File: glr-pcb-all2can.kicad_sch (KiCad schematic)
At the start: 0 parts

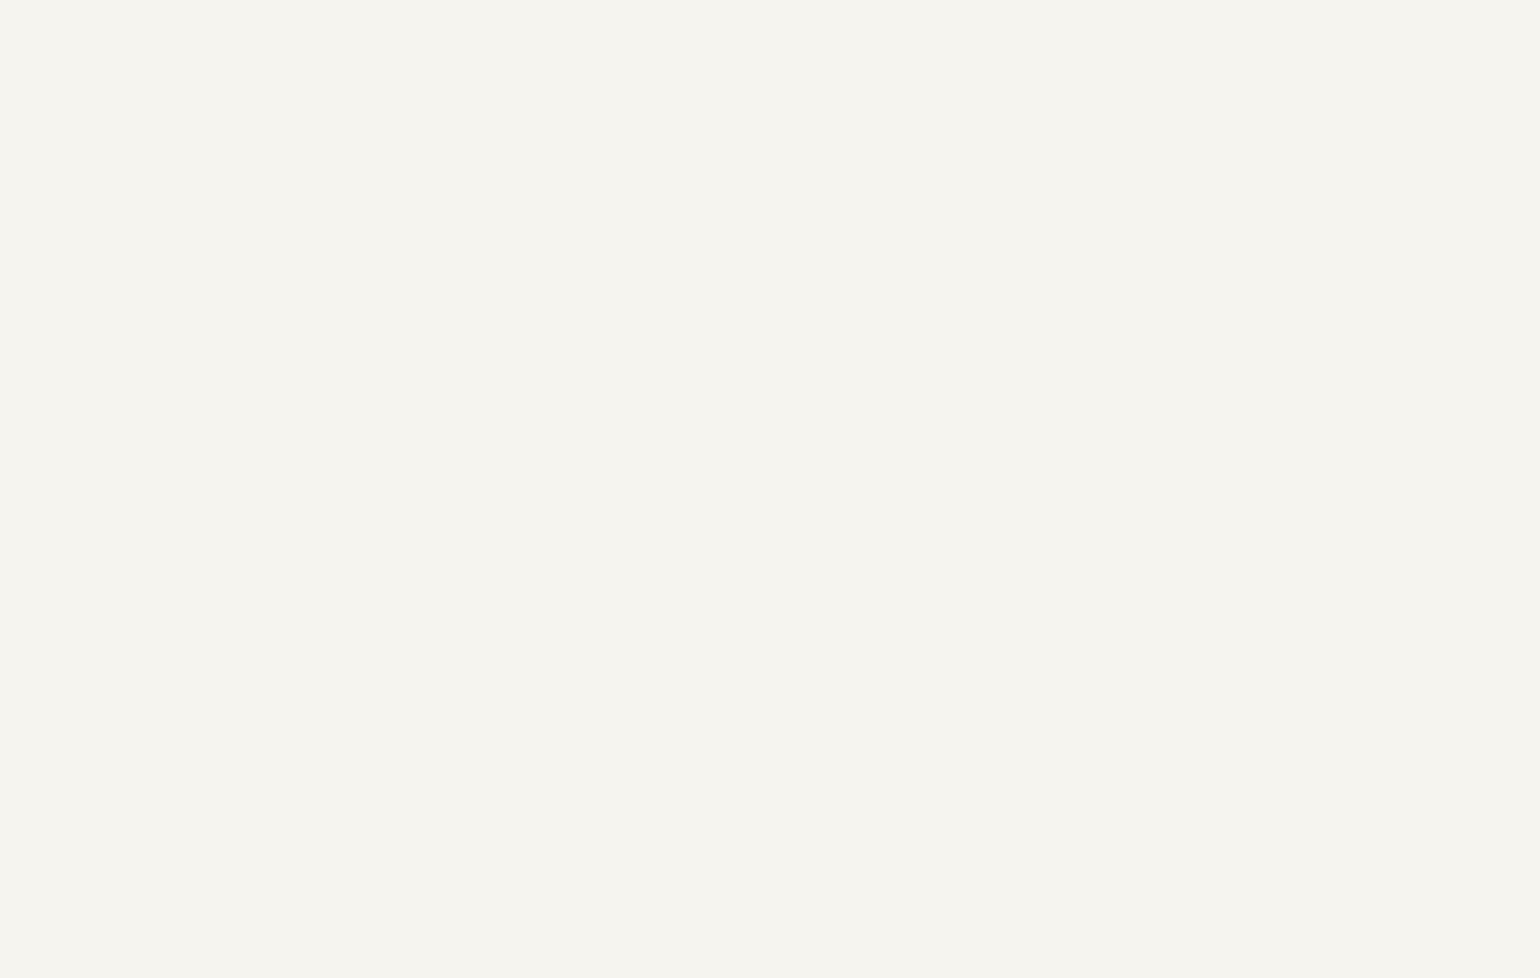
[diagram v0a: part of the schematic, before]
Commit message: add first can transcievers
update to glr-pcb-all2can references
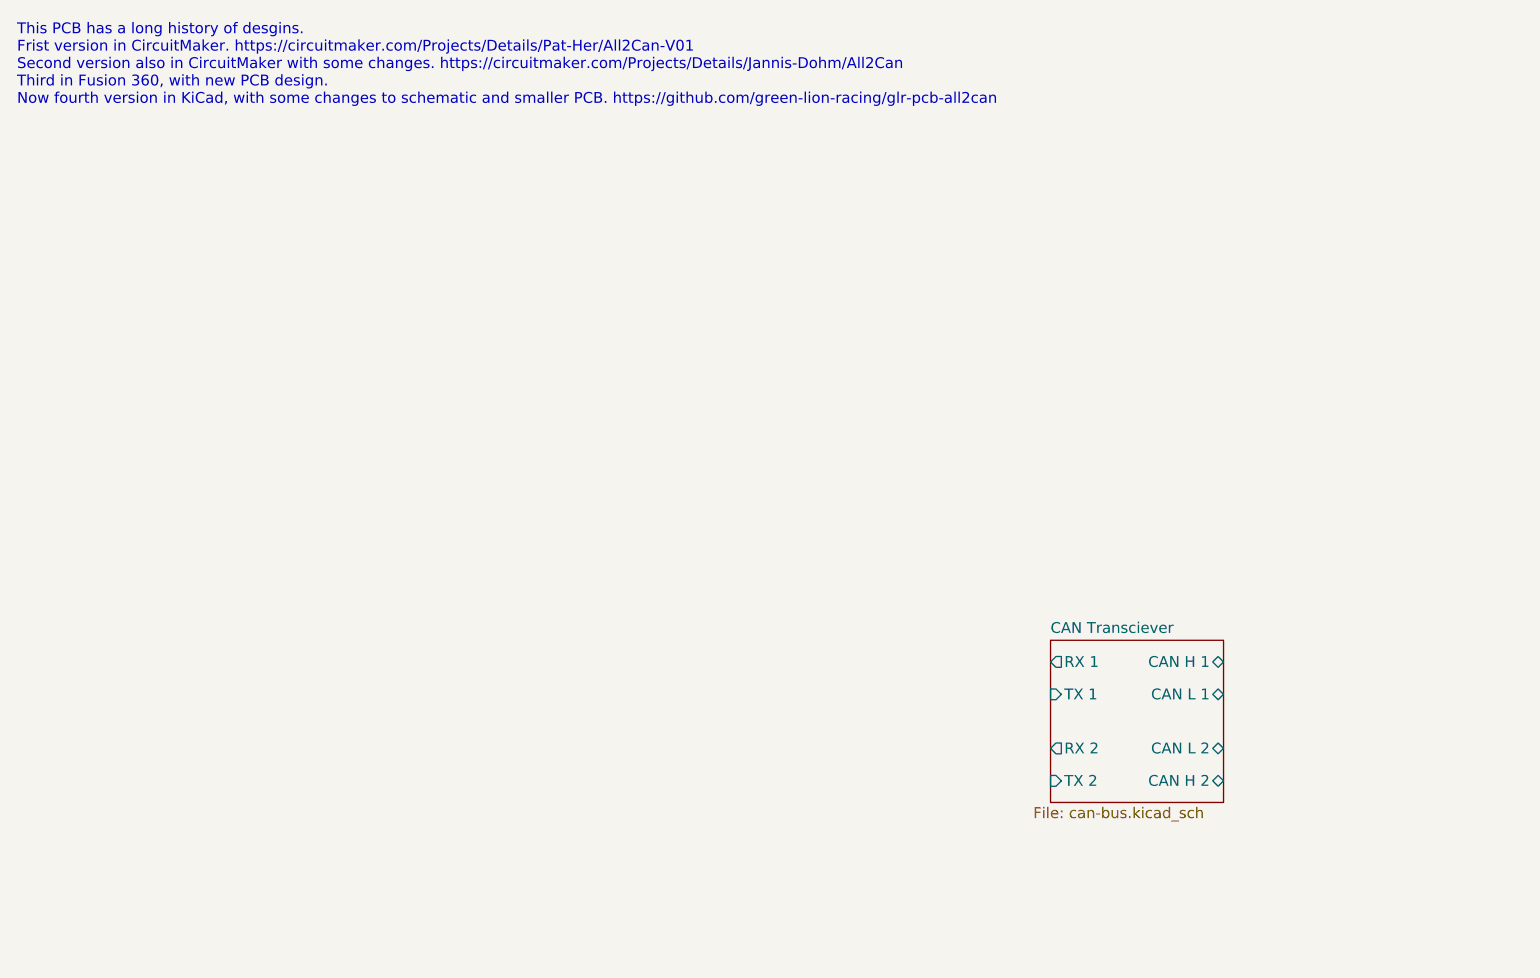
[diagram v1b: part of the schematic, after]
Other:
- added sheet CAN Transciever (can-bus.kicad_sch)
- note added: "This PCB has a long history of desgins. Frist version in CircuitMaker. https://circuitmaker.com/Projects/Details/Pat-Her/All2Can-V01 Second version also in CircuitMaker with some changes. https://circuitmaker.com/Projects/Details/Jannis-Dohm/All2Can Third in Fusion 360, with new PCB design. Now fourth version in KiCad, with some changes to schematic and smaller PCB. https://github.com/green-lion-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"
- title: SET A TITLE AND UPDATE AUTHOR FIELDS (DOUBLE CLICK HERE) -> All2Can
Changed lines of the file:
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@@
 	(paper "A4")
 	(title_block
-		(title "SET A TITLE AND UPDATE AUTHOR FIELDS (DOUBLE CLICK HERE)")
+		(title "All2Can")
 		(date "${CURRENT_DATE}")
-		(rev "v1")
+		(rev "v4")
 		(company "Green Lion Racing")
-		(comment 1 "Author #1")
-		(comment 2 "Author #2")
+		(comment 1 "Alexander Wallrodt")
+	)
+	(text "This PCB has a long history of desgins.\nFrist version in CircuitMaker. https://circuitmaker.com/Projects/Details/Pat-Her/All2Can-V01\nSecond version also in CircuitMaker with some changes. https://circuitmaker.com/Projects/Details/Jannis-Dohm/All2Can\nThird in Fusion 360, with new PCB design.\nNow fourth version in KiCad, with some changes to schematic and smaller PCB. https://github.com/green-lion-racing/glr-pcb-all2can"
+		(exclude_from_sim no)
+		(at 14.478 20.066 0)
+		(effects
+			(font
+				(size 1.27 1.27)
+			)
+			(justify left)
+		)
 	)
 	(symbol
@@
 				)
 			)
+		)
+	)
+	(sheet
+		(at 135.89 87.63)
+		(size 20.32 19.05)
+		(exclude_from_sim no)
+		(in_bom yes)
+		(on_board yes)
+		(dnp no)
+		(stroke
+			(width 0.1524)
+			(type solid)
+		)
+		(fill
+			(color 0 0 0 0.0000)
+		)
+		(property "Sheetname" "CAN Transciever"
+			(at 135.89 86.9184 0)
+			(effects
+				(font
+					(size 1.27 1.27)
+				)
+				(justify left bottom)
+			)
+		)
+		(property "Sheetfile" "can-bus.kicad_sch"
+			(at 133.858 107.188 0)
+			(effects
+				(font
+					(size 1.27 1.27)
+				)
+				(justify left top)
+			)
+		)
+		(pin "TX 1" input
+			(at 135.89 93.98 180)
+			(effects
+				(font
+					(size 1.27 1.27)
+				)
+				(justify left)
+			)
+		)
+		(pin "TX 2" input
+			(at 135.89 104.14 180)
+			(effects
+				(font
+					(size 1.27 1.27)
+				)
+				(justify left)
+			)
+		)
+		(pin "CAN H 1" bidirectional
+			(at 156.21 90.17 0)
+			(effects
+				(font
+					(size 1.27 1.27)
+				)
+				(justify right)
+			)
+		)
+		(pin "CAN L 1" bidirectional
+			(at 156.21 93.98 0)
+			(effects
+				(font
+					(size 1.27 1.27)
+				)
+				(justify right)
+			)
+		)
+		(pin "RX 1" output
+			(at 135.89 90.17 180)
+			(effects
+				(font
+					(size 1.27 1.27)
+				)
+				(justify left)
+			)
+		)
+		(pin "RX 2" output
+			(at 135.89 100.33 180)
+			(effects
+				(font
+					(size 1.27 1.27)
+				)
+				(justify left)
+			)
+		)
+		(pin "CAN L 2" bidirectional
+			(at 156.21 100.33 0)
+			(effects
+				(font
+					(size 1.27 1.27)
+				)
+				(justify right)
+			)
+		)
+		(pin "CAN H 2" bidirectional
+			(at 156.21 104.14 0)
+			(effects
+				(font
+					(size 1.27 1.27)
+				)
+				(justify right)
+			)
+		)
+		(instances
+			(project "glr-pcb-template"
+				(path "/be608b80-d1f2-4edd-b7a6-2b7cddd9f44f"
+					(page "2")
+				)
+			)

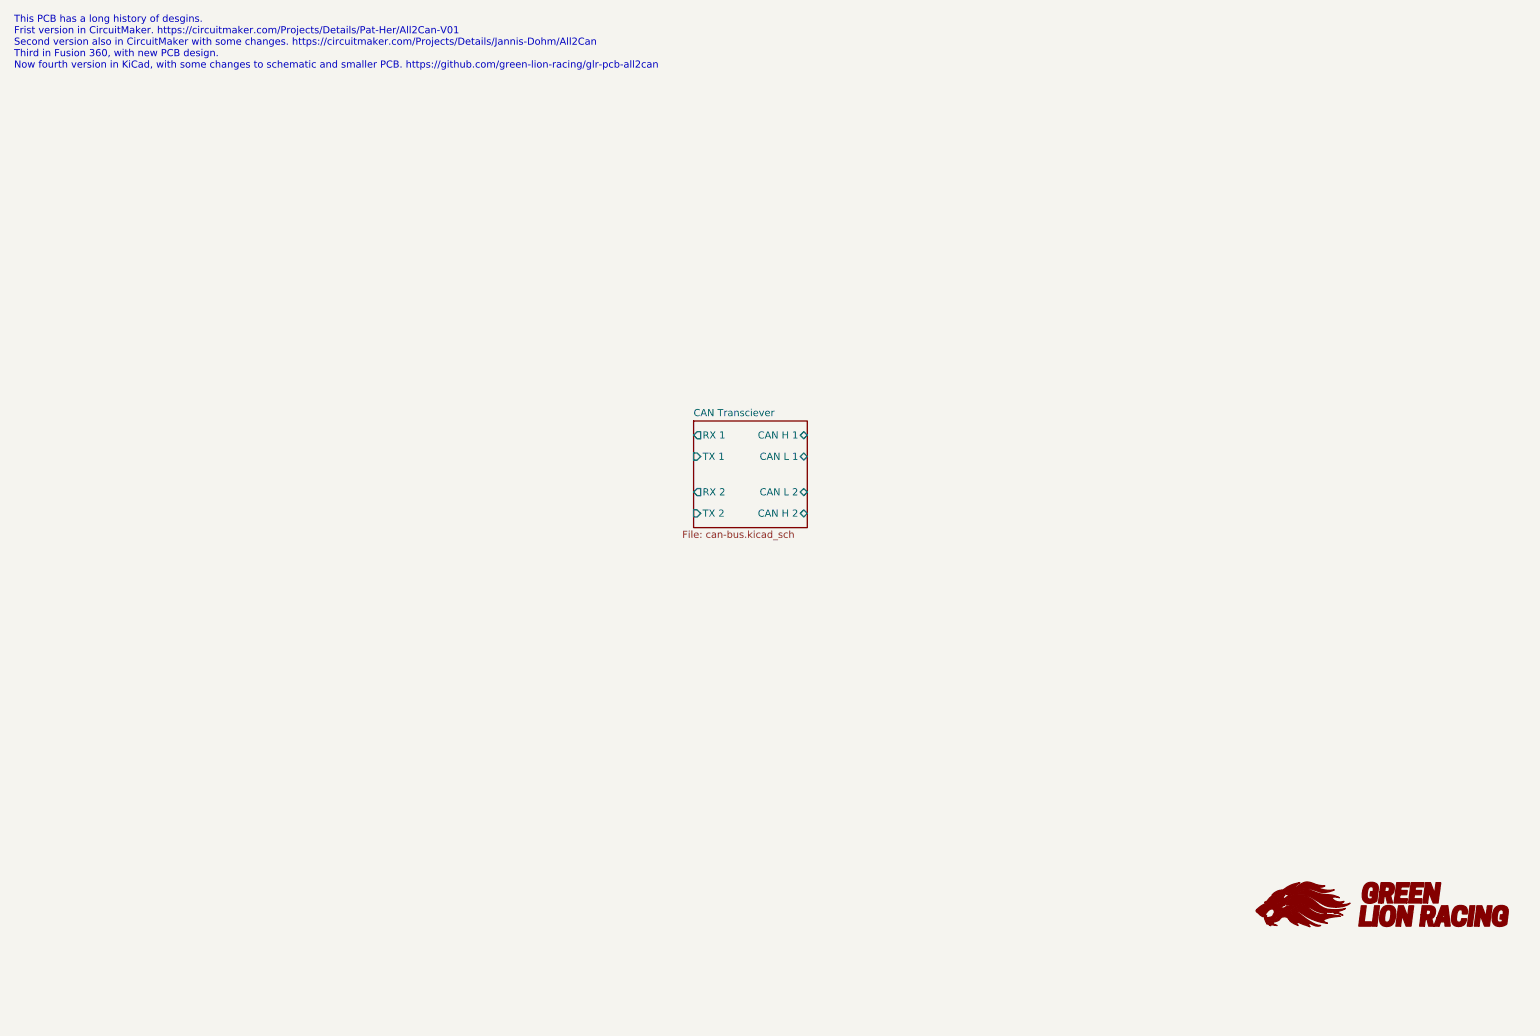
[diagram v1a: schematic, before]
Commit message: add main chip stm32f303k8t6
add two status leds
add debug/flash pins
connect first pins
remove second canbus
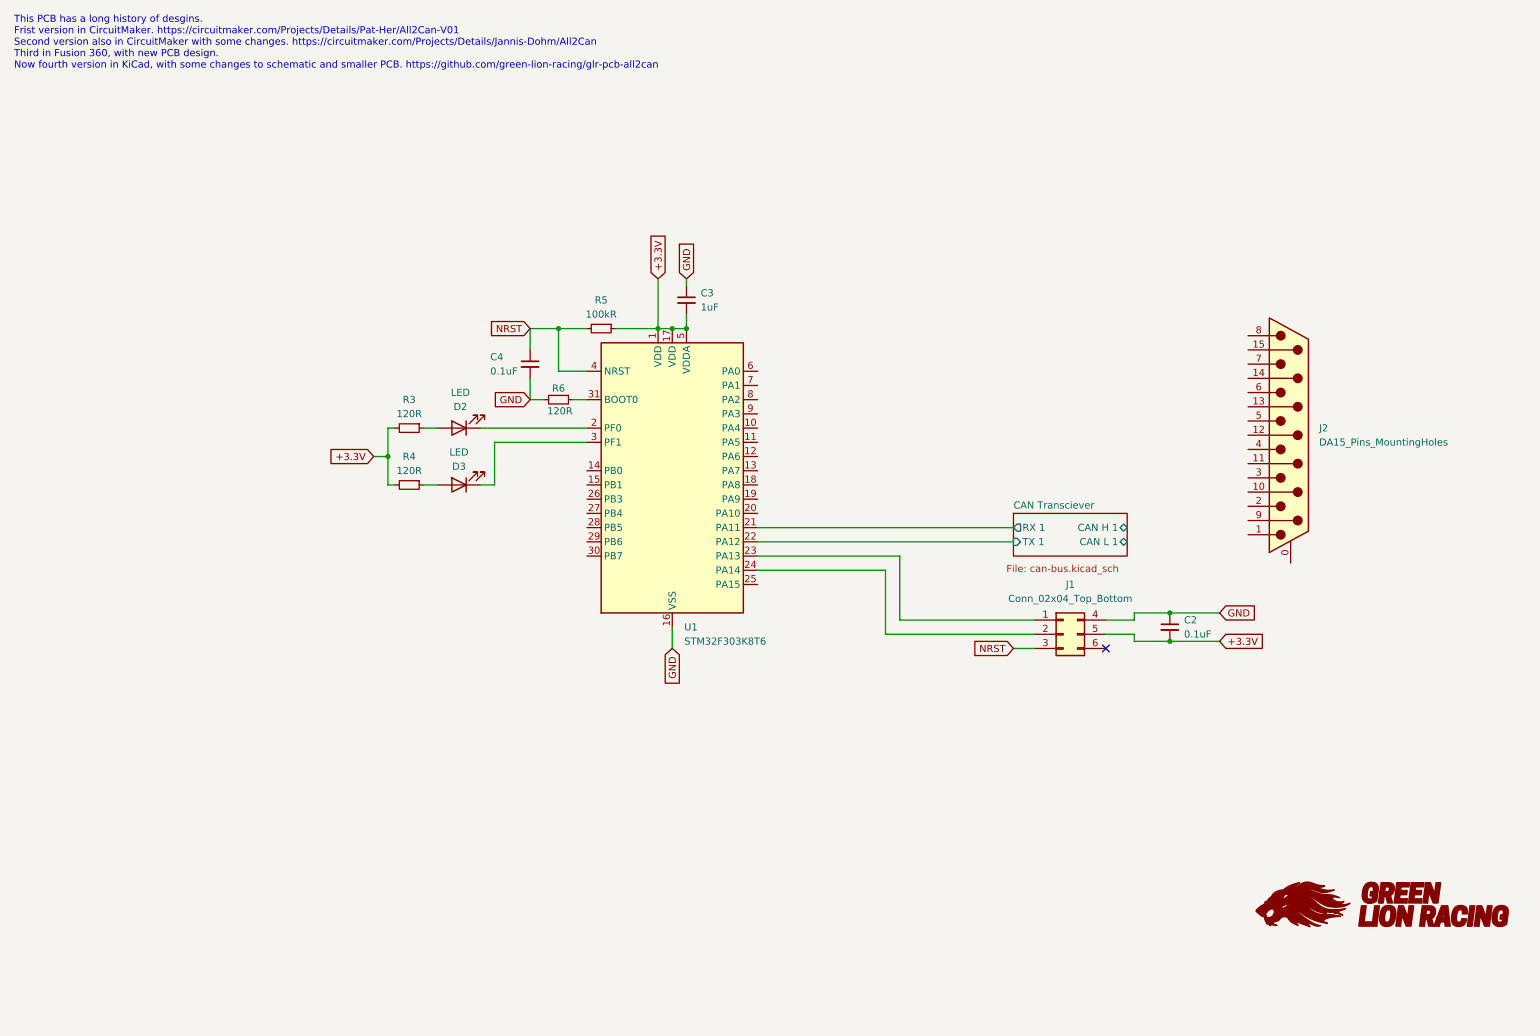
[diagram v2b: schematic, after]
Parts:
- added C2, C4: 0.1uF, symbol Device:C_Small
- added C3: 1uF, symbol Device:C_Small
- added D2, D3: LED, symbol Device:LED
- added J1: Conn_02x04_Top_Bottom, Connector_PinSocket_2.54mm:PinSocket_2x03_P2.54mm_Vertical, symbol Connector_Generic:Conn_02x03_Top_Bottom
- added J2: DA15_Pins_MountingHoles, Connector_Dsub:DSUB-15-HD_Pins_Horizontal_P2.29x1.90mm_EdgePinOffset3.03mm_Housed_MountingHolesOffset4.94mm, symbol Connector:DA15_Pins_MountingHoles
- added R3, R4, R6: 120R, symbol Device:R_Small
- added R5: 100kR, symbol Device:R_Small
- added U1: STM32F303K8T6, Package_QFP:LQFP-32_7x7mm_P0.8mm, symbol MCU_ST_STM32F3:STM32F303K8Tx
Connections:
- net CAN Transciever/RX 1: now also U1.21 (PA11)
- net CAN Transciever/TX 1: now also U1.22 (PA12)
- new net: D2.1 (K), U1.2 (PF0)
- new net: J1.1 (Pin_1), U1.23 (PA13)
- new net: J1.2 (Pin_2), U1.24 (PA14)
- new net: D3.1 (K), U1.3 (PF1)
- new net: R6.1, U1.31 (BOOT0)
- new net: D3.2 (A), R4.1
- new net: D2.2 (A), R3.1
- new net +3.3V: C2.2, C3.2, J1.5 (Pin_5), R3.2, R4.2, R5.1, U1.1 (VDD), U1.17 (VDD), U1.5 (VDDA)
- new net GND: C2.1, C3.1, C4.2, J1.4 (Pin_4), R6.2, U1.16 (VSS), U1.32 (VSS)
- new net NRST: C4.1, J1.3 (Pin_3), R5.2, U1.4 (NRST)
- no-connect marks 0 -> 1
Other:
- sheet CAN Transciever ports: added none; removed CAN H 2, CAN L 2, RX 2, TX 2

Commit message: add voltage converters by würth elektronik
add würth library
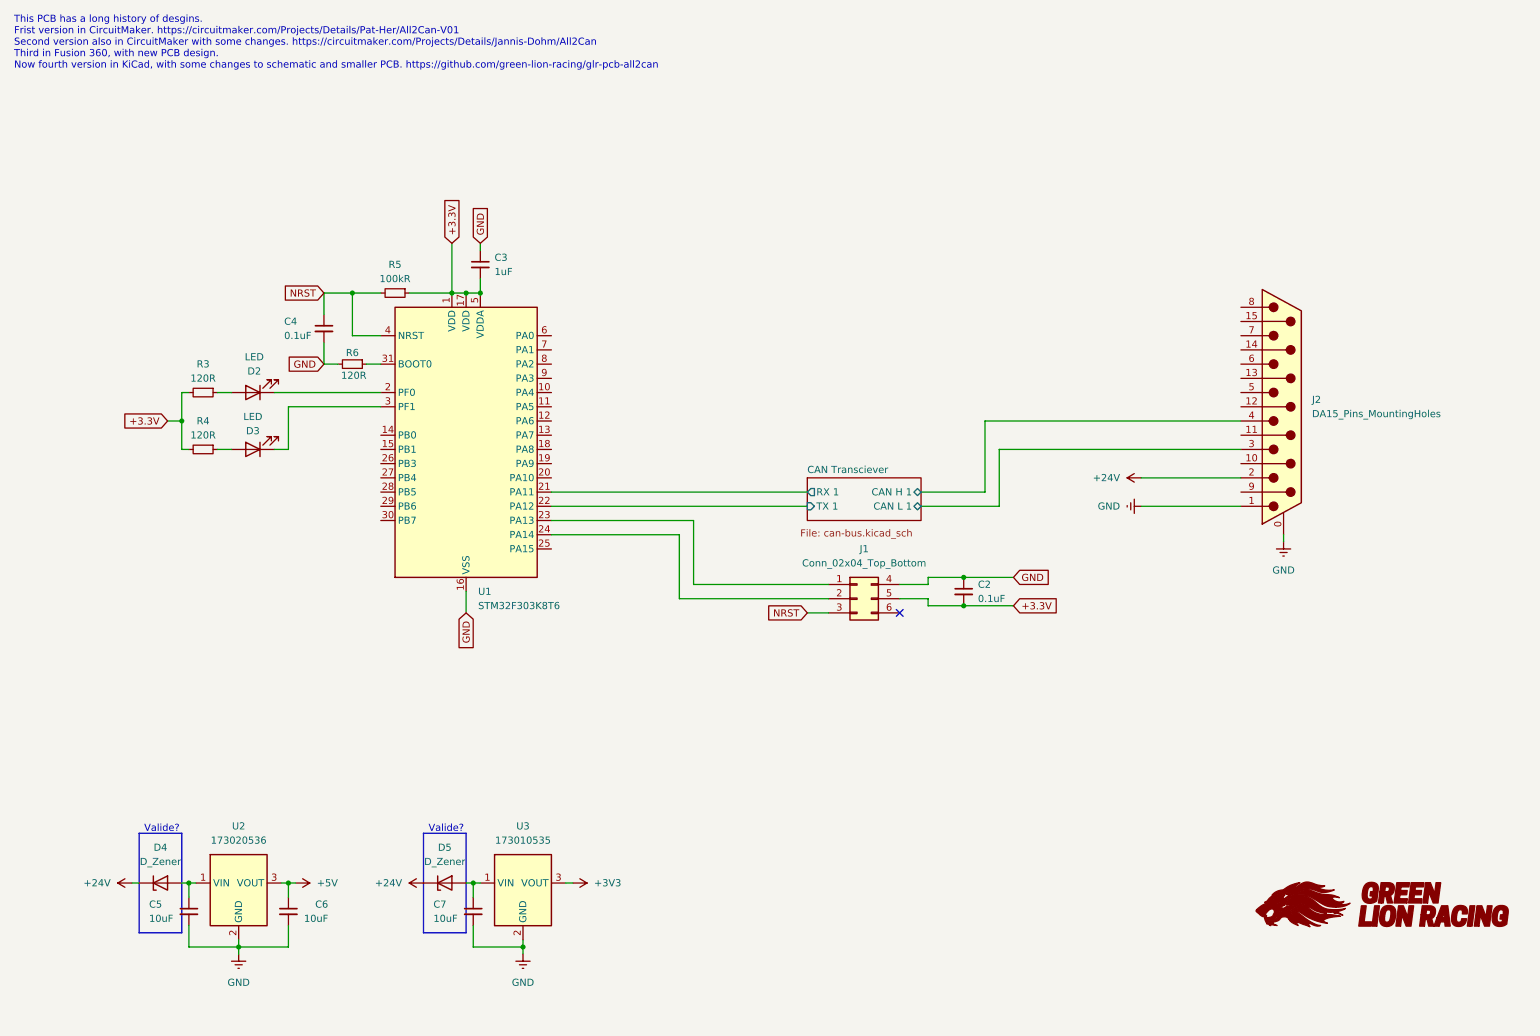
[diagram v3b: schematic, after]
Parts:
- added C5, C6, C7: 10uF, symbol Device:C_Small
- added D4, D5: D_Zener, symbol Device:D_Zener
- added U2: 173020536, MagIC_THT_Wurth:U_Wurth_MagIC-FDSM_17302xx36, symbol Würth MagIC FDSM:173020536
- added U3: 173010535, MagIC_THT_Wurth:U_Wurth_MagIC-FDSM_17301xx35, symbol Würth MagIC FDSM:173010535
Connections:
- net CAN Transciever/CAN H 1: now also J2.4
- net CAN Transciever/CAN L 1: now also J2.3
- net GND: now also J2.0 (PAD), J2.1, C5.2, C6.2, C7.2, U2.2 (GND), U3.2 (GND)
- net +24V: now reaches J2.2
- net +24V: now also D4.1 (K), D5.1 (K)
- new net: C5.1, D4.2 (A), U2.1 (VIN)
- new net: C7.1, D5.2 (A), U3.1 (VIN)
- new net +3V3: U3.3 (VOUT)
- new net +5V: C6.1, U2.3 (VOUT)
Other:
- note added: "Valide?"
- moved on the sheet: C2, C3, C4, D2, D3, J1, J2, R3, R4, R5, R6, U1
